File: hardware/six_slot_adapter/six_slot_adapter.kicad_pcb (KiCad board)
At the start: 2 copper layers, 100 x 100 mm, 21 parts, among them J3 CART SLOT TOP ROW, J4 CART SLOT BOTTOM ROW, M2_1 Screw_Terminal_01x01, M2_2 Screw_Terminal_01x01, M2_3 Screw_Terminal_01x01, M2_4 Screw_Terminal_01x01, M2_5 Screw_Terminal_01x01, M2_6 Screw_Terminal_01x01, M2_7 Screw_Terminal_01x01, M2_8 Screw_Terminal_01x01, M2_9 Screw_Terminal_01x01

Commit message: Add files via upload
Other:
- board text added: "OSCR SIX SLOT ADAPTER REV1 github.com/sanni/cartreader"
- board text removed: "3V3"
- board text removed: "5V"
- board text removed: "OSCR SIX SLOT ADAPTER HW4 REV1 github.com/sanni/cartreader"
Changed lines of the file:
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@@
     (effects (font (size 0.7 0.7) (thickness 0.15)) (justify mirror))
-  )
-  (gr_text "5V" (at 107.76 82.49 90) (layer "B.SilkS")
-    (effects (font (size 0.7 0.7) (thickness 0.125)) (justify left mirror))
   )
   (gr_text "D7" (at 181.635 53.582556 90) (layer "B.SilkS")
@@
     (effects (font (size 1 1) (thickness 0.15)) (justify mirror))
   )
-  (gr_text "3V3" (at 105.22 82.49 90) (layer "B.SilkS")
-    (effects (font (size 0.7 0.7) (thickness 0.125)) (justify left mirror))
-  )
   (gr_text "WR" (at 167.905 92.143 90) (layer "B.SilkS")
     (effects (font (size 0.7 0.7) (thickness 0.15)) (justify mirror))
@@
     (effects (font (size 0.7 0.7) (thickness 0.15)) (justify mirror))
   )
-  (gr_text "5V" (at 186.17 140.57 90) (layer "B.SilkS")
+  (gr_text "VCC" (at 186.17 140.57 90) (layer "B.SilkS")
     (effects (font (size 0.7 0.7) (thickness 0.15)) (justify mirror))
   )
@@
     (effects (font (size 0.7 0.7) (thickness 0.15)) (justify mirror))
   )
-  (gr_text "5V" (at 187.41 124.665 90) (layer "B.SilkS")
+  (gr_text "VCC" (at 187.41 124.665 90) (layer "B.SilkS")
     (effects (font (size 0.7 0.7) (thickness 0.15)) (justify mirror))
   )
@@
     (effects (font (size 0.7 0.7) (thickness 0.125)) (justify left mirror))
   )
-  (gr_text "5V" (at 187.39 75.775 90) (layer "B.SilkS")
+  (gr_text "VCC" (at 187.39 75.775 90) (layer "B.SilkS")
     (effects (font (size 0.7 0.7) (thickness 0.15)) (justify mirror))
   )
@@
     (effects (font (size 0.7 0.7) (thickness 0.15)) (justify mirror))
   )
-  (gr_text "5V" (at 142.99 140.41 90) (layer "B.SilkS")
+  (gr_text "VCC" (at 142.99 140.41 90) (layer "B.SilkS")
     (effects (font (size 0.7 0.7) (thickness 0.15)) (justify mirror))
   )
@@
     (effects (font (size 0.7 0.7) (thickness 0.15)) (justify mirror))
   )
-  (gr_text "OSCR SIX SLOT ADAPTER\nHW4 REV1\ngithub.com/sanni/cartreader" (at 103.46 128.385 90) (layer "B.SilkS")
+  (gr_text "OSCR SIX SLOT ADAPTER\nREV1\ngithub.com/sanni/cartreader" (at 103.46 128.385 90) (layer "B.SilkS")
     (effects (font (size 1 1) (thickness 0.15)) (justify mirror))
   )
@@
     (effects (font (size 0.7 0.7) (thickness 0.15)) (justify mirror))
   )
-  (gr_text "5V" (at 113.73 70.162556 90) (layer "B.SilkS")
-    (effects (font (size 0.7 0.7) (thickness 0.15)) (justify mirror))
-  )
+  (gr_text "VCC" (at 113.73 70.162556 90) (layer "B.SilkS")
+    (effects (font (size 0.7 0.7) (thickness 0.15)) (justify mirror))
+  )

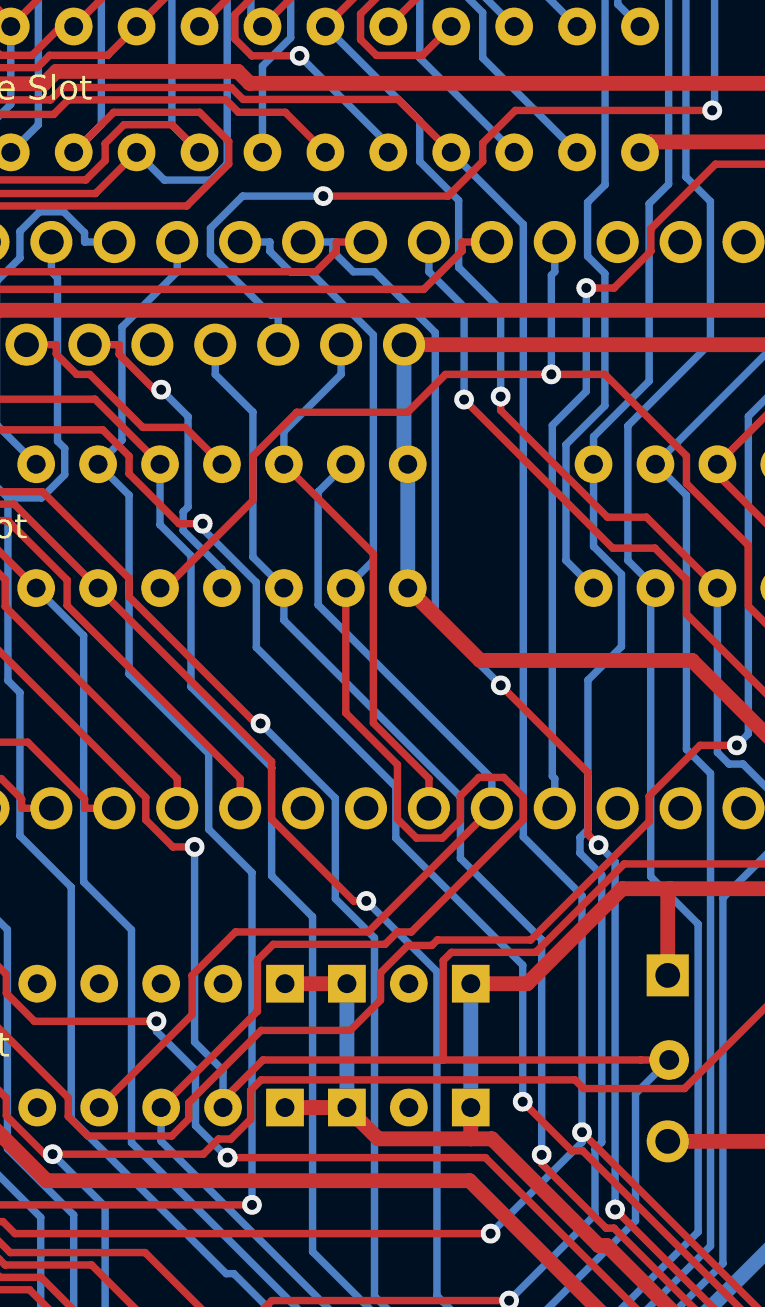
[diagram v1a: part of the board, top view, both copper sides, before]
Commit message: Add Six Slot Adapter Rev2 (fixes CIC Reset)
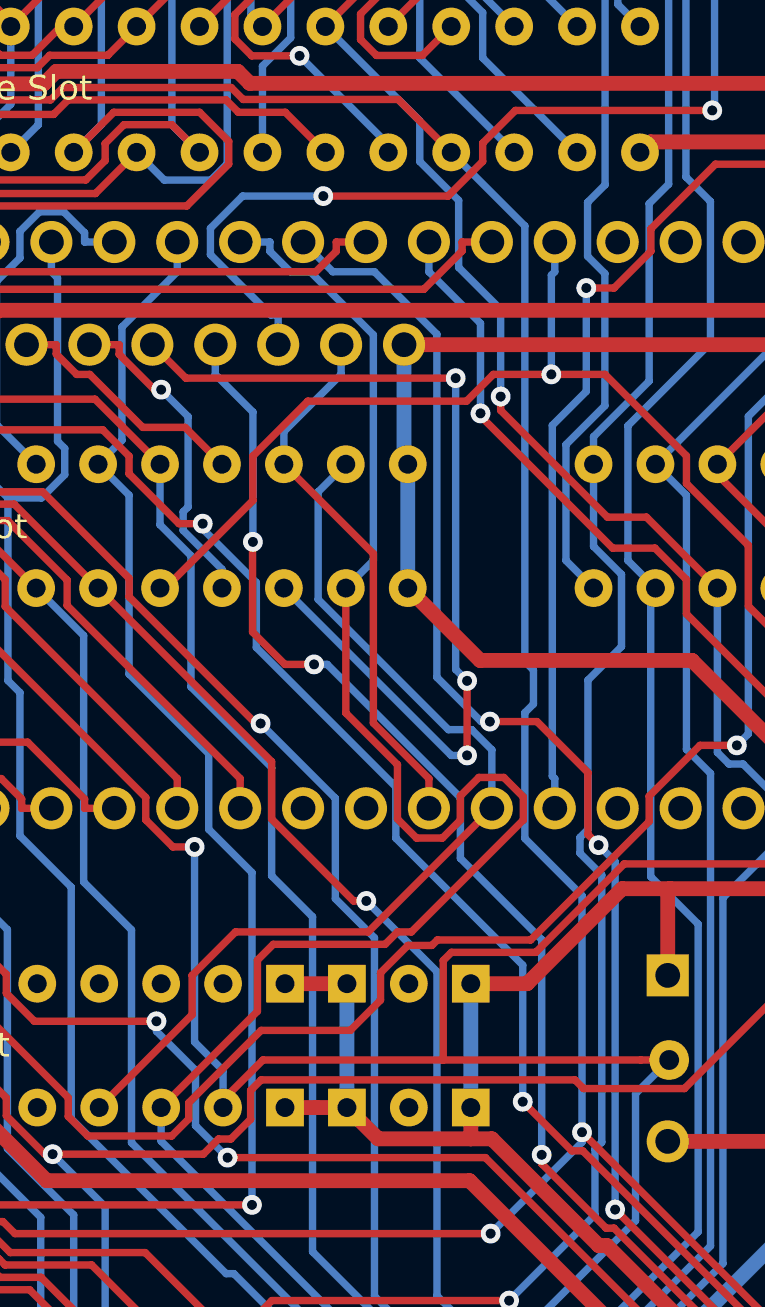
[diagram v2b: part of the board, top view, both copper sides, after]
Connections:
- J3 pad 2: +3V3 -> unconnected-(J3-Pad2)
- J3 pad 3: +5V -> unconnected-(J3-Pad3)
- J3 pad 34: D53 -> unconnected-(J3-Pad34)
- J3 pad 35: D52 -> unconnected-(J3-Pad35)
- J3 pad 36: D51 -> unconnected-(J3-Pad36)
- J3 pad 37: D50 -> unconnected-(J3-Pad37)
- J4 pad 2: D0 -> unconnected-(J4-Pad2)
- J4 pad 28: D20 -> unconnected-(J4-Pad28)
- J4 pad 29: D21 -> unconnected-(J4-Pad29)
- J4 pad 3: D1 -> unconnected-(J4-Pad3)
- J4 pad 33: D13 -> unconnected-(J4-Pad33)
- J4 pad 34: D38 -> unconnected-(J4-Pad34)
- J4 pad 35: RESET -> unconnected-(J4-Pad35)
- SNES1 pad 25: D40 -> CIC RESET
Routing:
- net CIC RESET: track 0.00 -> 38.4 mm, vias 0 -> 3
- net D16: track 135.2 -> 136.4 mm
- net D40: track 154.2 -> 155.2 mm, vias 4 -> 6
- net CLK1: track 39.0 -> 39.6 mm
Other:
- board text added: "OSCR SIX SLOT ADAPTER REV2 github.com/sanni/cartreader"
- board text removed: "OSCR SIX SLOT ADAPTER REV1 github.com/sanni/cartreader"

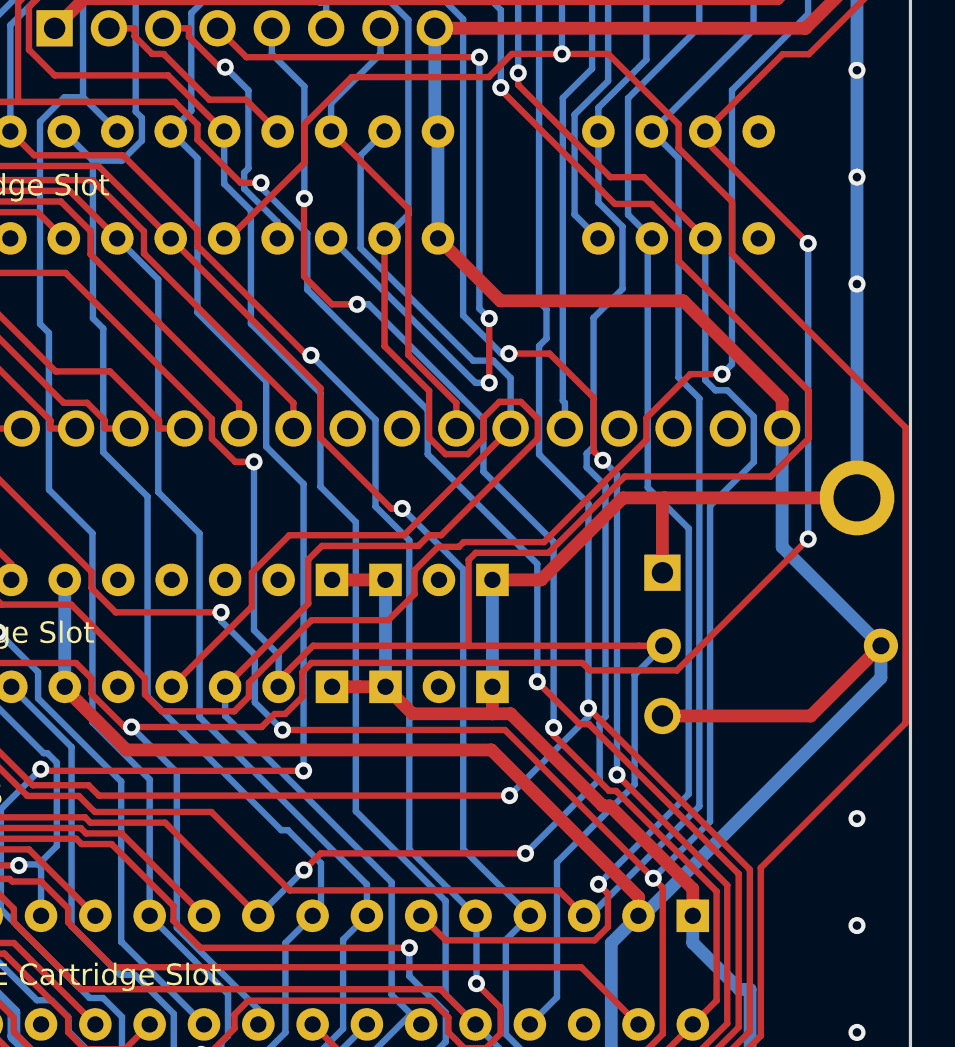
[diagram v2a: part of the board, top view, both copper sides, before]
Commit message: Change N64 controller connector pitch to 2.54mm
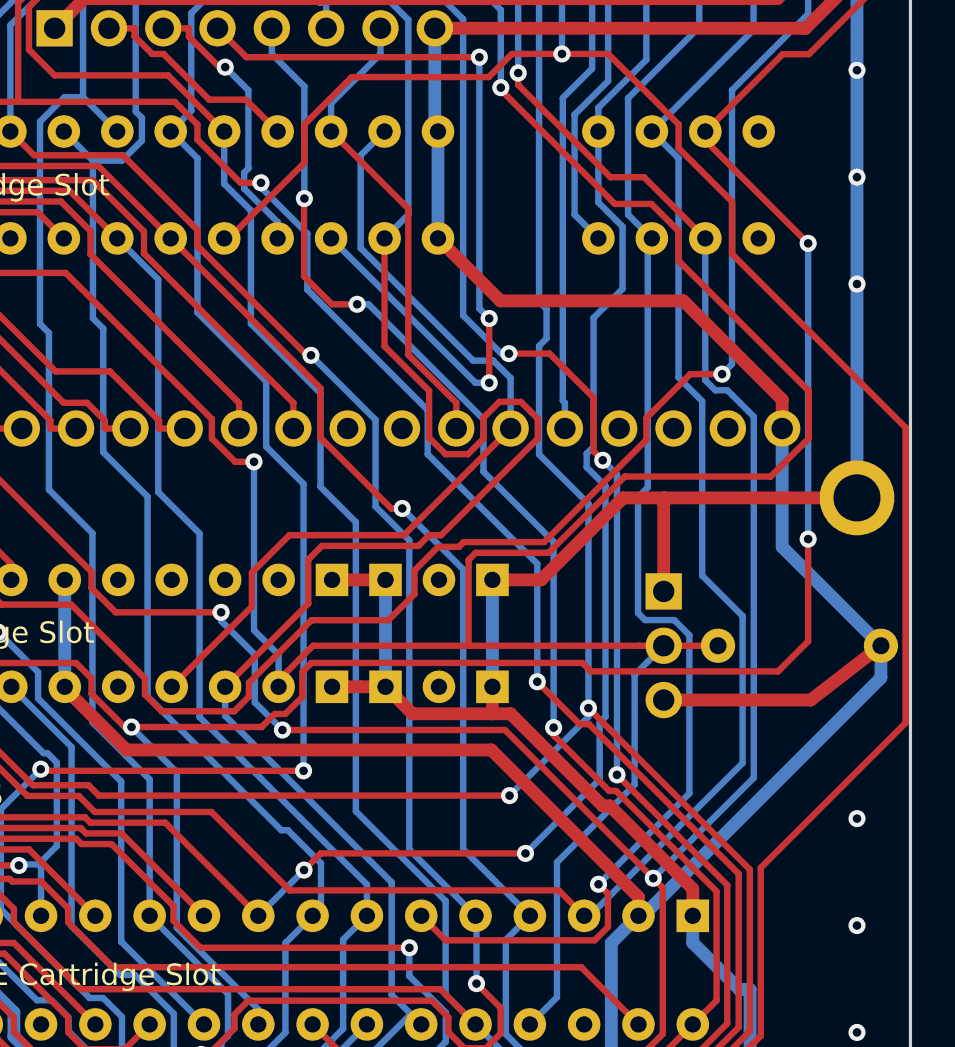
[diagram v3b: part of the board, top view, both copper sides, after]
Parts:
- added JC2: Conn_01x01, Connector_PinHeader_2.54mm:PinHeader_1x01_P2.54mm_Vertical, F.Cu at (188.5, 114.4)
- moved R1 2.54 mm to (201.2, 114.4)
- moved JC3 0.88 mm to (188.5, 111.9)
- moved JC1 0.75 mm to (188.5, 117.0)
- renumbered JC2 to JC3
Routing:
- net D27: track 236.0 -> 238.9 mm
- net D7: track 122.5 -> 125.0 mm
- net D25: track 250.0 -> 251.7 mm
- net D24: track 232.1 -> 233.3 mm
- net GND: track 522.6 -> 523.4 mm
- net VCC: track 375.2 -> 374.6 mm
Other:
- board text added: "OSCR SIX SLOT ADAPTER REV3 github.com/sanni/cartreader"
- board text removed: "OSCR SIX SLOT ADAPTER REV2 github.com/sanni/cartreader"

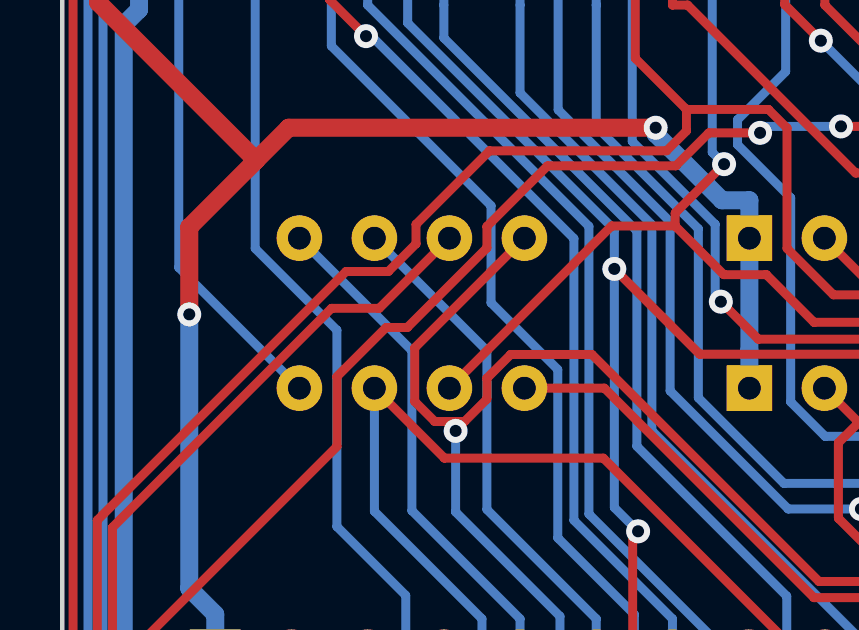
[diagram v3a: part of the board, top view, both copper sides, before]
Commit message: Minor fixes/changes to six-slot adapter and git repository
* Add JLCPCB order ID text to Six-Slot Adapter; you can select "specify location" for order number location when ordering from JLCPCB. It is placed so the SNES slot covers it. (PCB revision not incremented because it is only a minor change to the silkscreen.)
* Added relative path for footprint and symbol libs to six-slot adapter project files.
* Added footprint details/links to schematic symbols.
* Added .gitignore and included most of the files that should remain local-only.
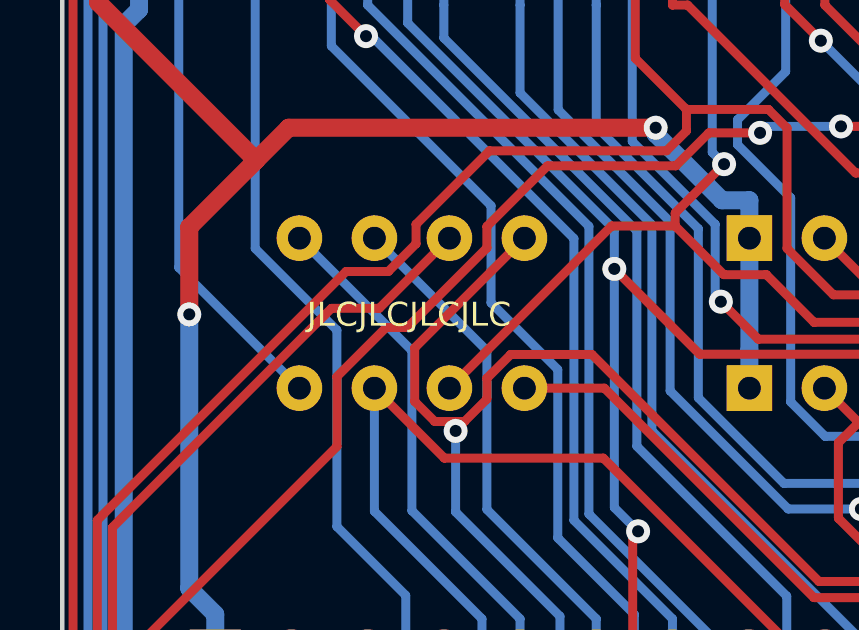
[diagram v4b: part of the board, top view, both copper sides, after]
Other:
- board text added: "JLCJLCJLCJLC"
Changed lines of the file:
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@@
       (effects (font (size 1 1) (thickness 0.15)))
     )
+    (fp_line (start 1.27 -1.27) (end 1.27 1.27) (layer "F.Fab") (width 0.1))
     (fp_line (start 1.27 1.27) (end -1.27 1.27) (layer "F.Fab") (width 0.1))
     (fp_line (start -0.635 -1.27) (end 1.27 -1.27) (layer "F.Fab") (width 0.1))
-    (fp_line (start 1.27 -1.27) (end 1.27 1.27) (layer "F.Fab") (width 0.1))
     (fp_line (start -1.27 -0.635) (end -0.635 -1.27) (layer "F.Fab") (width 0.1))
     (fp_line (start -1.27 1.27) (end -1.27 -0.635) (layer "F.Fab") (width 0.1))
@@
     (effects (font (size 1 1) (thickness 0.15)))
   )
+  (gr_text "JLCJLCJLCJLC" (at 111.56 92.915) (layer "F.SilkS")
+    (effects (font (size 0.8 0.8) (thickness 0.15)))
+  )
   (gr_text "2.54mm 64-Pin MEGA DRIVE Cartridge Slot" (at 152.99 129.815) (layer "F.SilkS")

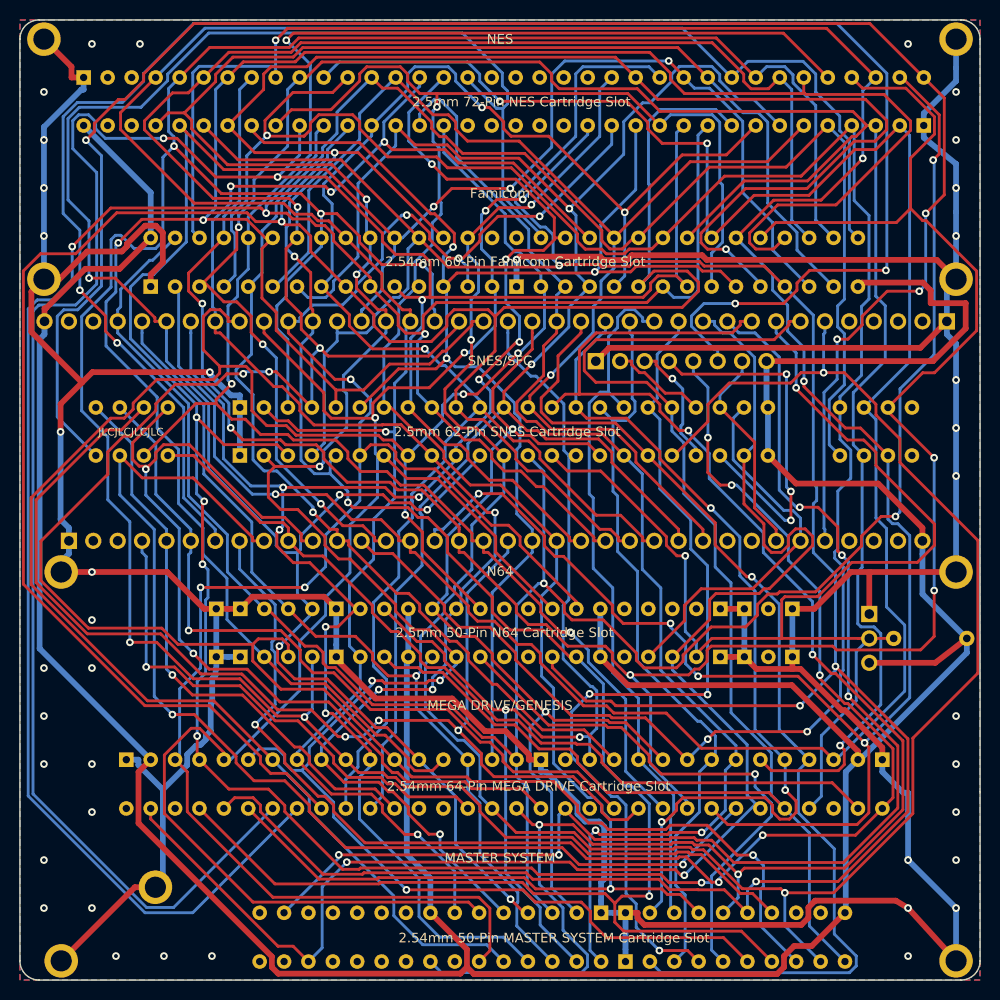
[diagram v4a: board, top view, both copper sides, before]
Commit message: Add 12V rail for N64 + silkscreen updates
Add a 12V rail for the N64 slot. This is not currently implemented, but as the six-slot adapter is the hardest of the 2 boards to upgrade having it now will save some effort for anyone wanting it in the future. It also makes it easier to externally supply 12V by attaching clips to the 12V and GND header pins.

Also improved the silkscreen a bit to match the main PCB.
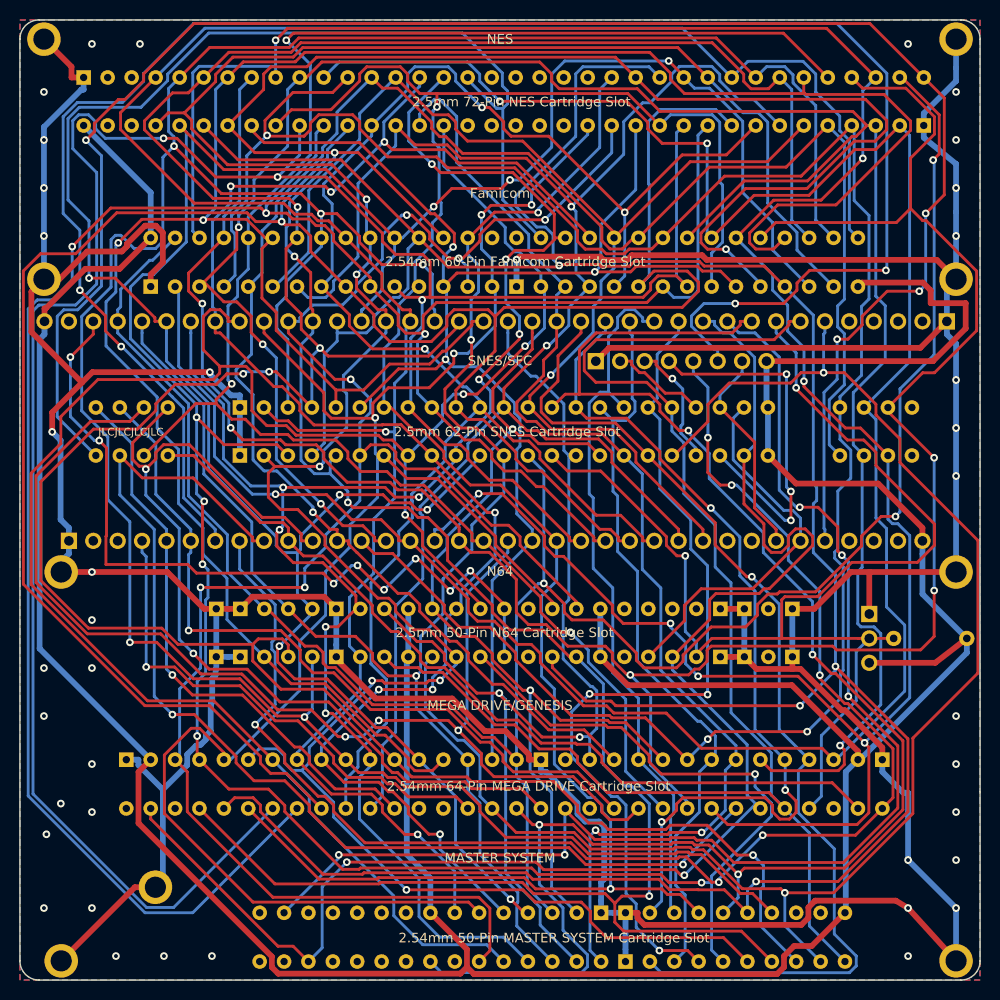
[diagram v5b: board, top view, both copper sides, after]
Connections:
- J3 pad 3: unconnected-(J3-Pad3) -> +12V
- N64 pad 13: unconnected-(N64-Pad13) -> +12V
- N64 pad 38: unconnected-(N64-Pad38) -> +12V
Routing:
- net +12V: track 0.00 -> 82.8 mm, vias 0 -> 8
- net A5: track 204.9 -> 207.7 mm
- net A14: track 299.8 -> 302.1 mm
- net D37: track 108.1 -> 110.2 mm
- net D36: track 100.9 -> 102.4 mm
- net A6: track 183.6 -> 185.1 mm
- net D29: track 121.6 -> 123.1 mm
- net A1: track 168.2 -> 169.2 mm
- net D27: track 238.9 -> 239.7 mm
- net A3: track 175.1 -> 175.9 mm
- net GND: track 523.4 -> 524.1 mm
- net A7: track 197.3 -> 197.8 mm
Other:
- board text added: "12V"
- board text added: "OSCR SIX-SLOT ADAPTER github.com/sanni/cartreader"
- board text added: "REV${REVISION}"
- board text removed: "OSCR SIX SLOT ADAPTER REV3 github.com/sanni/cartreader"
